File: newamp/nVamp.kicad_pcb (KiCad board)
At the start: 4 copper layers, 44.2 x 31 mm, 26 parts, among them J1 CONN_01X02, J2 CONN_01X03, J3 CONN_01X02, J4 CONN_01X02, U1 AD8428, U2 ADA4528, U3 ADA4528, U4 AD8428

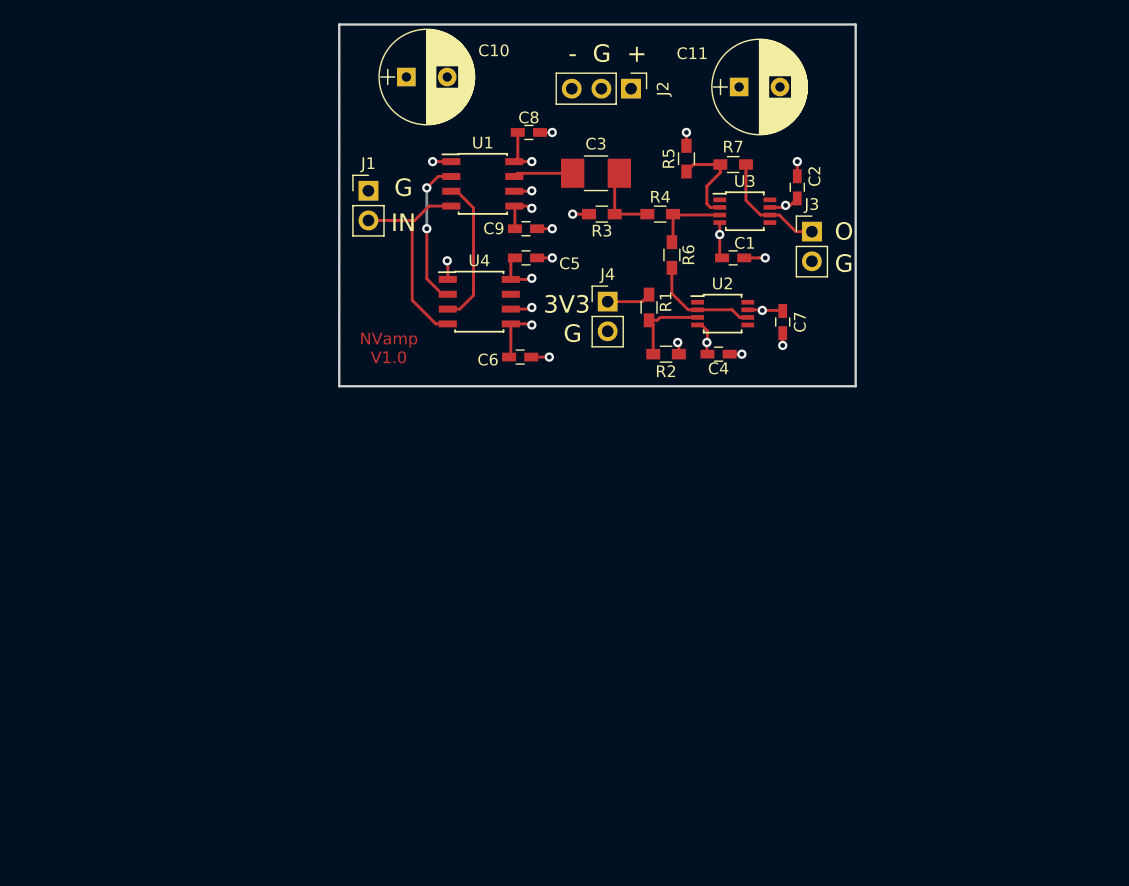
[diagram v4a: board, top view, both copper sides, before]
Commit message: Begin working on v2 pcb
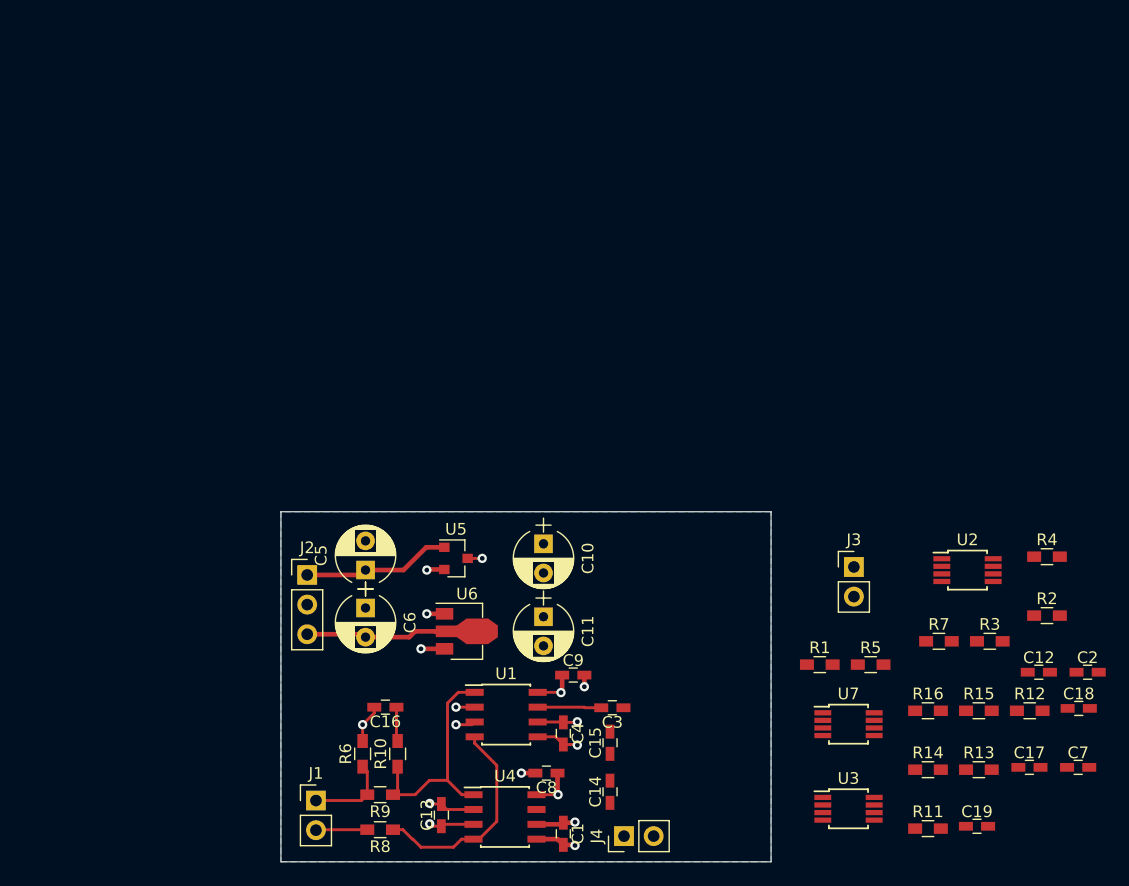
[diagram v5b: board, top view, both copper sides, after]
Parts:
- added C12: 5n, Capacitors_SMD:C_0603_HandSoldering, F.Cu at (174.9, 103.8)
- added C13: 5n, Capacitors_SMD:C_0603_HandSoldering, F.Cu at (123.8, 116.0)
- added C14: 100n, Capacitors_SMD:C_0603_HandSoldering, F.Cu at (138.2, 114.0)
- added C15: 100n, Capacitors_SMD:C_0603_HandSoldering, F.Cu at (138.2, 109.8)
- added C16: 100n, Capacitors_SMD:C_0603_HandSoldering, F.Cu at (119.0, 106.8)
- added C17: 500n, Capacitors_SMD:C_0603_HandSoldering, F.Cu at (174.1, 111.9)
- added C18: 31n, Capacitors_SMD:C_0603_HandSoldering, F.Cu at (178.4, 106.9)
- added C19: 31n, Capacitors_SMD:C_0603_HandSoldering, F.Cu at (169.6, 117.0)
- added R10: 100, Resistors_SMD:R_0603_HandSoldering, F.Cu at (120.0, 110.8)
- added R11: 100, Resistors_SMD:R_0603_HandSoldering, F.Cu at (165.4, 117.2)
- added R12: 1k, Resistors_SMD:R_0603_HandSoldering, F.Cu at (174.2, 107.1)
- added R13: 100, Resistors_SMD:R_0603_HandSoldering, F.Cu at (169.8, 112.1)
- added R14: 1k, Resistors_SMD:R_0603_HandSoldering, F.Cu at (165.4, 112.1)
- added R15: 100, Resistors_SMD:R_0603_HandSoldering, F.Cu at (169.8, 107.1)
- added R16: 1k, Resistors_SMD:R_0603_HandSoldering, F.Cu at (165.4, 107.1)
- added R8: 100, Resistors_SMD:R_0603_HandSoldering, F.Cu at (118.5, 117.2)
- added R9: 100, Resistors_SMD:R_0603_HandSoldering, F.Cu at (118.5, 114.2)
- added U5: L7805, TO_SOT_Packages_SMD:SOT-23, F.Cu at (125.0, 94.0)
- added U6: L7905, TO_SOT_Packages_SMD:SOT-89-3, F.Cu at (125.5, 100.2)
- added U7: ADA4528-2, Housings_SSOP:MSOP-8_3x3mm_Pitch0.65mm, F.Cu at (158.6, 108.2)
- C10, C11: value CP -> 10u; footprint Capacitors_THT:CP_Radial_D8.0mm_P3.50mm -> Capacitors_THT:CP_Radial_D5.0mm_P2.50mm
- C3: value 100u -> 100n; footprint Capacitors_SMD:C_1210_HandSoldering -> Capacitors_SMD:C_0603_HandSoldering
- C5, C6: value 100n -> 1u; footprint Capacitors_SMD:C_0603_HandSoldering -> Capacitors_THT:CP_Radial_D5.0mm_P2.50mm
- C7: value 100n -> 31n
- R3: value 15k -> 2k
- R4: value 100 -> 15k
- R6: value 33k -> 10k
- R7: value 33k -> 1k
- U2, U3: value ADA4528 -> ADA4528-2; footprint Housings_SSOP:TSSOP-8_3x3mm_Pitch0.65mm -> Housings_SSOP:MSOP-8_3x3mm_Pitch0.65mm
- moved C8 54.9 mm to (132.8, 112.4), turned to 180 degrees
- moved J1 52.4 mm to (113.0, 114.8)
- moved U3 52.0 mm to (158.6, 115.5)
- moved C1 51.5 mm to (134.2, 117.6), turned to 270 degrees
- moved R6 50.3 mm to (117.0, 110.8), turned to 90 degrees
- moved J2 50.1 mm to (112.2, 95.4), turned to 0 degrees
- moved R3 49.4 mm to (170.7, 101.1), turned to 0 degrees
- moved C2 48.4 mm to (179.1, 103.8), turned to 0 degrees
- moved C11 48.4 mm to (132.5, 99.0), turned to 270 degrees
- moved R5 46.1 mm to (160.5, 103.1), turned to 0 degrees
- moved C3 45.8 mm to (138.4, 106.8)
- moved J4 45.8 mm to (139.4, 117.8), turned to 90 degrees
- moved C7 45.8 mm to (178.3, 111.9), turned to 0 degrees
- moved U1 45.5 mm to (129.3, 107.4)
- moved R7 44.5 mm to (166.4, 101.1), turned to 0 degrees
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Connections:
- C5 pad 1: GND -> Net-(C5-Pad1)
- C5 pad 2: VEE -> GND
- C6 pad 2: VEE -> Net-(C6-Pad2)
- C7 pad 1: VDD -> Net-(C17-Pad2)
- C7 pad 2: GND -> Net-(C7-Pad2)
- J1 pad 1: GND -> Net-(J1-Pad1)
- J1 pad 2: /IN+ -> Net-(J1-Pad2)
- J2 pad 1: VDD -> Net-(C5-Pad1)
- J2 pad 3: VEE -> Net-(C6-Pad2)
- J3 pad 1: Net-(J3-Pad1) -> Net-(C19-Pad1)
- R3 pad 2: GND -> /VRef
- R4 pad 2: Net-(R4-Pad2) -> Net-(C12-Pad2)
- R5 pad 1: GND -> /VRef
- R6 pad 1: Net-(R4-Pad2) -> Net-(J1-Pad1)
- R6 pad 2: /VRef -> GND
- R7 pad 1: Net-(J3-Pad1) -> Net-(R11-Pad1)
- U1 pad 1: GND -> /IN-
- U2 pad 1: (no net) -> /VRef
- U2 pad 4: VEE -> GND
- U2 pad 6: /VRef -> (no net)
- U2 pad 7: VDD -> (no net)
- U2 pad 8: (no net) -> VDD
- U3 pad 1: (no net) -> Net-(R11-Pad1)
- U3 pad 3: Net-(R4-Pad2) -> Net-(C12-Pad2)
- U3 pad 4: VEE -> GND
- U3 pad 5: (no net) -> /VRef
- U3 pad 6: Net-(J3-Pad1) -> Net-(C7-Pad2)
- U3 pad 7: VDD -> Net-(C17-Pad2)
- U3 pad 8: (no net) -> VDD
- U4 pad 1: GND -> /IN-
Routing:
- net Net-(C6-Pad2): track 0.00 -> 23.7 mm
- net /IN-: track 0.00 -> 19.8 mm
- net Net-(C5-Pad1): track 0.00 -> 12.7 mm
- net Net-(J3-Pad1): track 9.83 -> 0.00 mm
- net /VRef: track 9.70 -> 0.00 mm
- net Net-(R5-Pad2): track 8.22 -> 0.00 mm
- net Net-(C14-Pad2): track 7.31 -> 0.00 mm
- net Net-(J1-Pad1): track 0.00 -> 7.17 mm
- net Net-(R4-Pad2): track 6.47 -> 0.00 mm
- net Net-(C3-Pad1): track 6.47 -> 0.00 mm
- net VDD: track 13.9 -> 8.52 mm, vias 4 -> 3
- net VEE: track 14.5 -> 9.24 mm, vias 4 -> 3
- net GND: track 20.5 -> 15.6 mm, vias 15 -> 7
- net Net-(J1-Pad2): track 0.00 -> 4.42 mm
- net +3V3: track 3.79 -> 0.00 mm
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- added copper zone on B.Cu, net GND
- added copper zone on In1.Cu, net VDD
- added copper zone on In2.Cu, net VEE
- removed copper zone on In1.Cu, net GND
- removed copper zone on In2.Cu, net VDD
- removed copper zone on B.Cu, net VEE
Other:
- board size 44.2 x 31 mm -> 42 x 30 mm
- board text removed: "+"
- board text removed: "-"
- board text removed: "3V3"
- board text removed: "G"
- board text removed: "IN"
- board text removed: "NVamp V1.0"
- board text removed: "O"

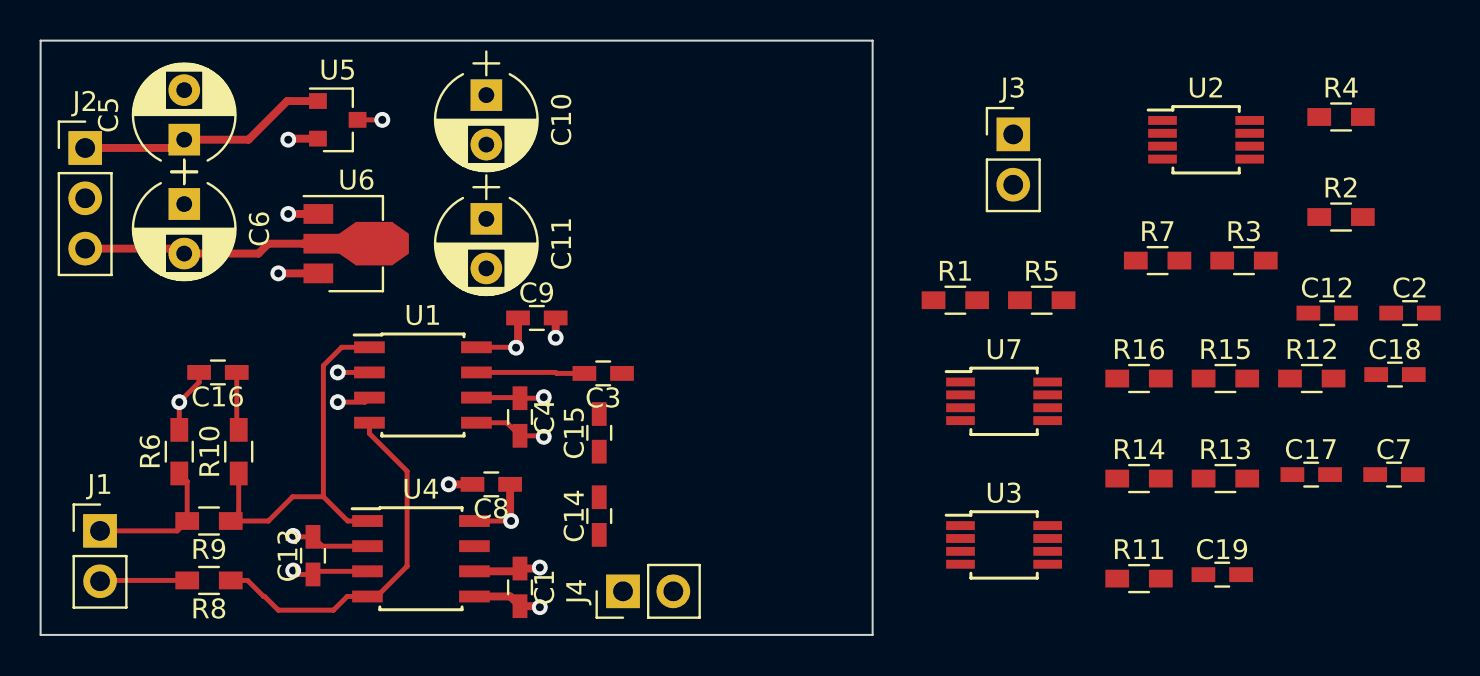
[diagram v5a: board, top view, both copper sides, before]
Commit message: Finished version 2.0 of the amplifier PCB
Add better filtering from Ben,
Add differential input
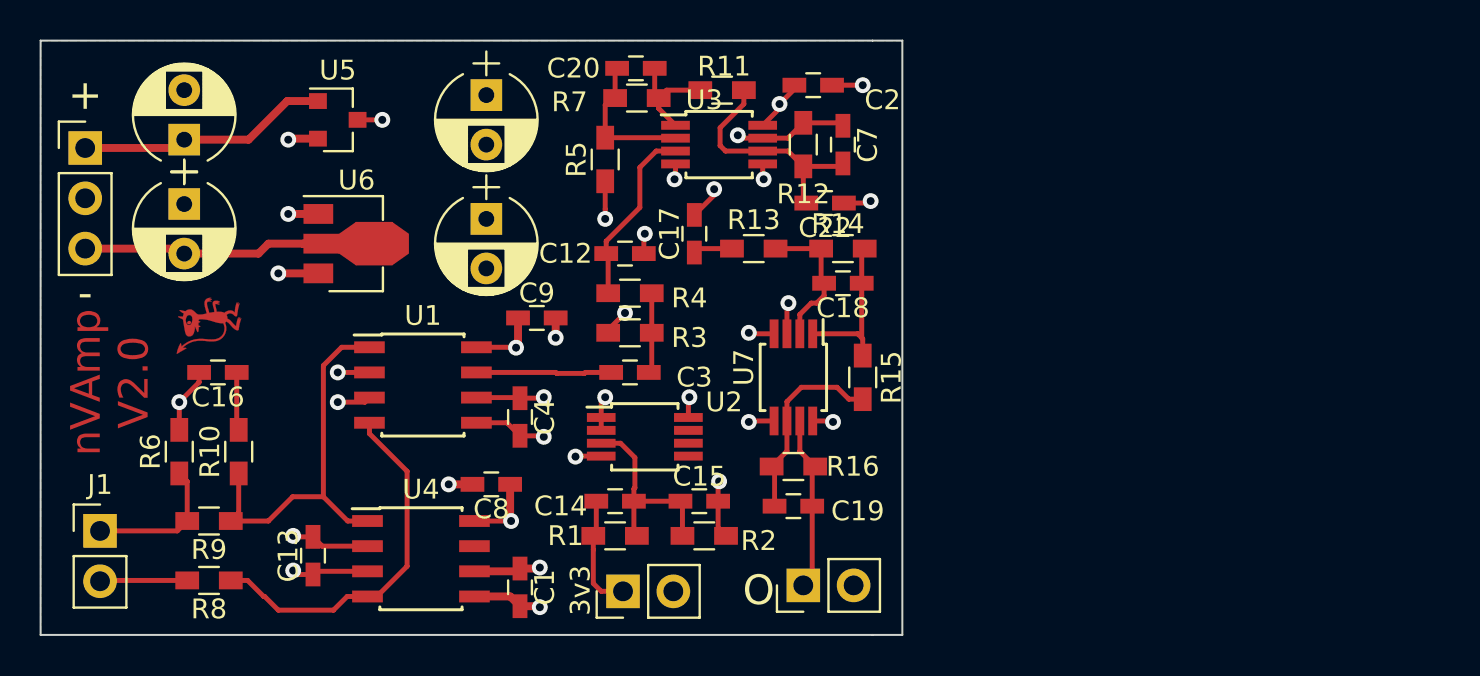
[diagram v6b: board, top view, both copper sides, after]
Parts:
- added C20: 62n, Capacitors_SMD:C_0603_HandSoldering, F.Cu at (140.1, 91.4)
- added C22: 620n, Capacitors_SMD:C_0603_HandSoldering, F.Cu at (149.6, 98.2)
- added G***: luci, w_conn_av:luci, F.Cu at (118.5, 104.4)
- C18, C7: value 31n -> 62n
- R12, R14: value 1k -> 1.2k
- R16: value 1k -> 2k
- moved R4 37.0 mm to (139.8, 102.8), turned to 180 degrees
- moved R2 35.9 mm to (143.5, 115.0)
- moved C12 35.6 mm to (139.5, 100.8), turned to 180 degrees
- moved C17 33.4 mm to (143.0, 99.8), turned to 90 degrees
- moved C7 32.4 mm to (150.5, 95.2), turned to 270 degrees
- moved R11 32.4 mm to (144.4, 92.5)
- moved C2 32.2 mm to (149.0, 92.2)
- moved U2 32.1 mm to (140.5, 110.0)
- moved R3 31.2 mm to (139.8, 104.8), turned to 180 degrees
- moved R12 28.3 mm to (148.5, 95.2), turned to 270 degrees
- moved C18 28.2 mm to (150.5, 102.2), turned to 180 degrees
- moved R7 27.5 mm to (140.1, 92.9), turned to 180 degrees
- moved R13 26.5 mm to (146.0, 100.5)
- moved J3 25.1 mm to (148.5, 117.5), turned to 90 degrees
- moved U3 24.8 mm to (144.2, 95.2)
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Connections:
- net Net-(C17-Pad2) renamed /intermediate
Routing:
- net Net-(C22-Pad2): track 0.00 -> 11.9 mm
- net /intermediate: track 0.00 -> 10.7 mm, vias 0 -> 2
- net Net-(C14-Pad2): track 0.00 -> 10.2 mm
- net Net-(C19-Pad2): track 0.00 -> 10.0 mm
- net /VRef: track 0.00 -> 9.70 mm, vias 0 -> 7
- net GND: track 15.6 -> 24.9 mm, vias 7 -> 13
- net Net-(C12-Pad2): track 0.00 -> 9.24 mm
- net Net-(C19-Pad1): track 0.00 -> 8.87 mm
- net Net-(C18-Pad1): track 0.00 -> 8.04 mm
- net Net-(C20-Pad2): track 0.00 -> 7.46 mm
- net Net-(C18-Pad2): track 0.00 -> 7.33 mm
- net +3V3: track 0.00 -> 5.88 mm
- net Net-(C20-Pad1): track 0.00 -> 5.58 mm
- net VDD: track 8.52 -> 13.3 mm, vias 3 -> 6
- net Net-(C3-Pad1): track 0.00 -> 4.06 mm
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- added copper zone on In2.Cu, net /VRef
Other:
- board size 42 x 30 mm -> 43.5 x 30 mm
- board text added: "+"
- board text added: "-"
- board text added: "3v3"
- board text added: "O"
- board text added: "nVAmp V2.0"

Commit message: Lots of changes
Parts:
- removed C16: 100n, Capacitors_SMD:C_0603_HandSoldering
- removed R10: 100, Resistors_SMD:R_0603_HandSoldering
- removed R6: 10k, Resistors_SMD:R_0603_HandSoldering
- R15: value 100 -> 1k
- U5: value L7805 -> MCP1700-1202E_SOT23
- moved G*** 2.47 mm to (119.1, 106.8)
- moved U5 0.50 mm to (125.4, 94.3), turned to 180 degrees
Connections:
- J1 pad 1: Net-(J1-Pad1) -> GND
- R9 pad 2: Net-(J1-Pad1) -> GND
- U5 pad 1: Net-(C5-Pad1) -> GND
- U5 pad 2: GND -> VDD
- U5 pad 3: VDD -> Net-(C5-Pad1)
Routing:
- net Net-(J1-Pad1): track 7.17 -> 0.00 mm
- net VDD: track 13.3 -> 18.4 mm, vias 6 -> 5
- net Net-(C16-Pad1): track 2.94 -> 0.00 mm
- net GND: track 24.9 -> 27.6 mm
- net /IN-: track 19.8 -> 17.2 mm
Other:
- board text added: "nVAmp V2.1"
- board text removed: "nVAmp V2.0"
